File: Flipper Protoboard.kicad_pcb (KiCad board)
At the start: 2 copper layers, 71.1 x 45.7 mm, 394 parts

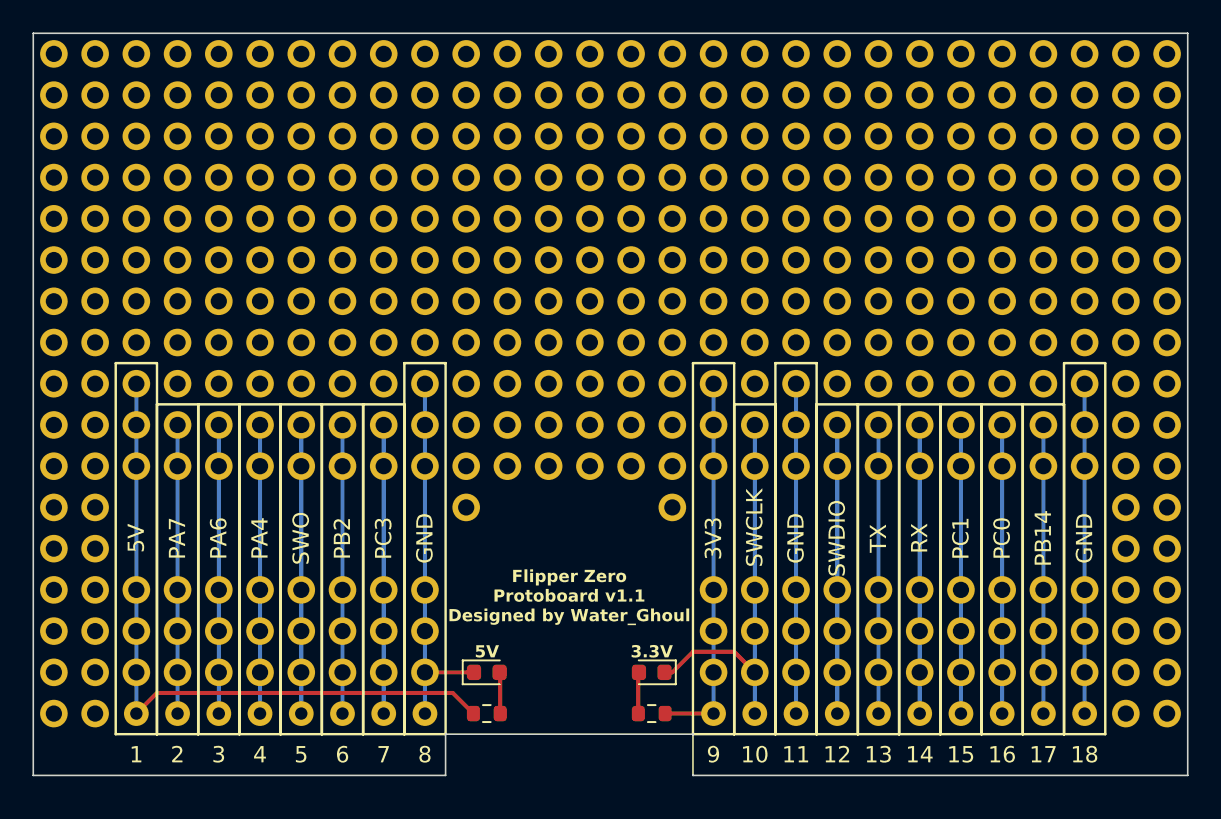
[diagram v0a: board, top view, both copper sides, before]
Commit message: Added new PCB flie
Added a few minor tweaks to update the board to v1.2
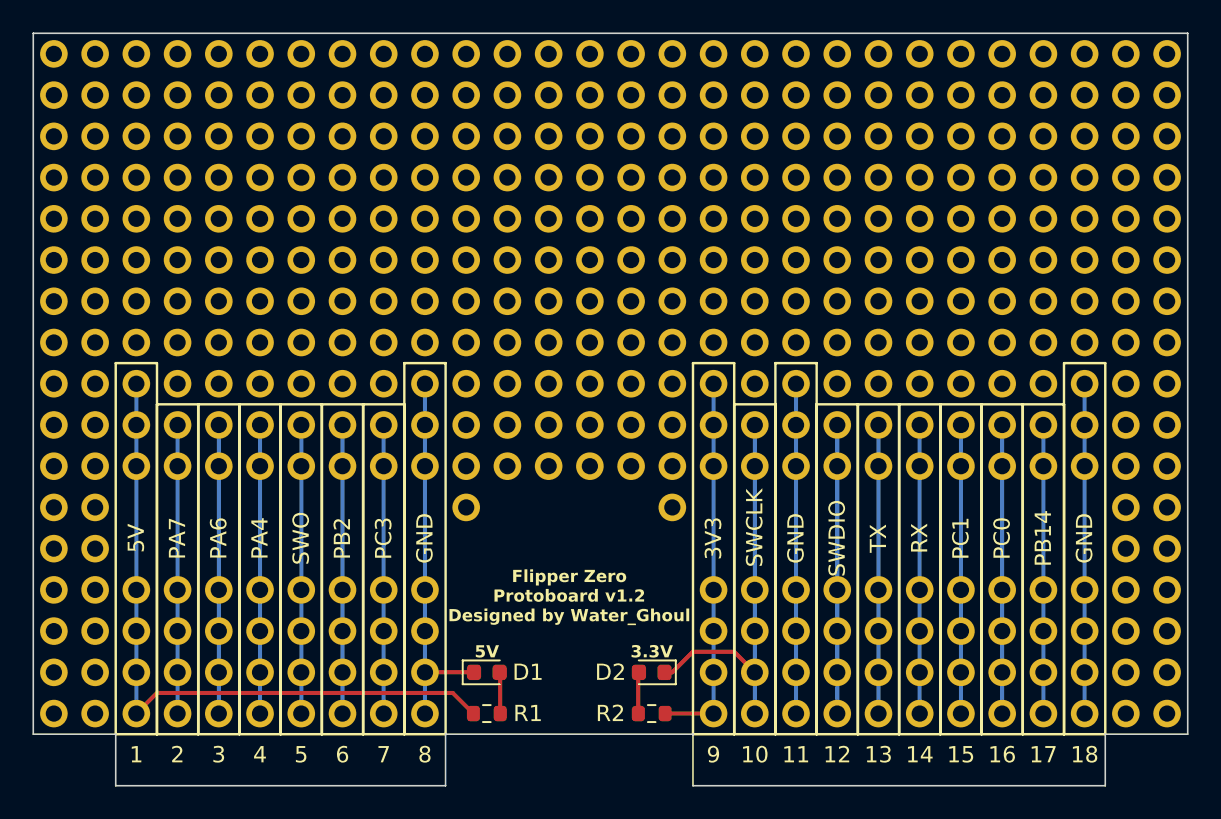
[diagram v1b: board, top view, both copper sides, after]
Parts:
- removed REF**: Flipper Zero GPIO, 1 My Parts:Flipper Zero GPIO
- added J1: PinHeader_1x08_P2.54mm_Horizontal, Connector_PinHeader_2.54mm:PinHeader_1x08_P2.54mm_Horizontal, B.Cu at (68.6, 139.7)
- added J2: PinHeader_1x10_P2.54mm_Horizontal, Connector_PinHeader_2.54mm:PinHeader_1x10_P2.54mm_Horizontal, B.Cu at (104.1, 139.7)
- renumbered REF** to D1, REF** to D2, REF** to R1, REF** to R2
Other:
- board size 71.1 x 45.7 mm -> 71.1 x 46.4 mm
- board text added: "Flipper Zero Protoboard v1.2 Designed by Water_Ghoul"
- board text removed: "Flipper Zero Protoboard v1.1 Designed by Water_Ghoul"

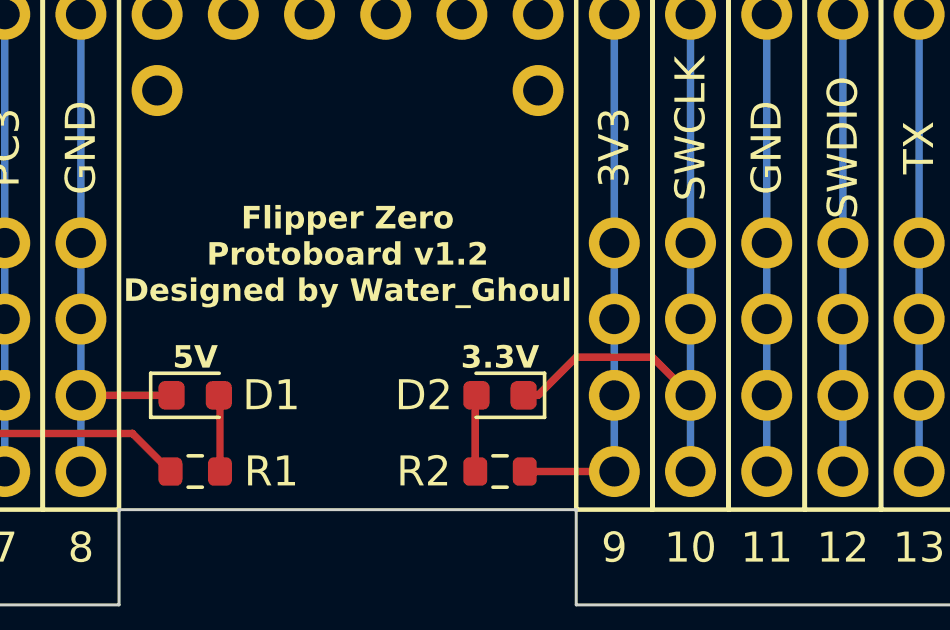
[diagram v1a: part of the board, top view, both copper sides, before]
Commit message: Fixed 3V3 LED
Fixed the 3V3 indicator LED grounded to to wrong pin.
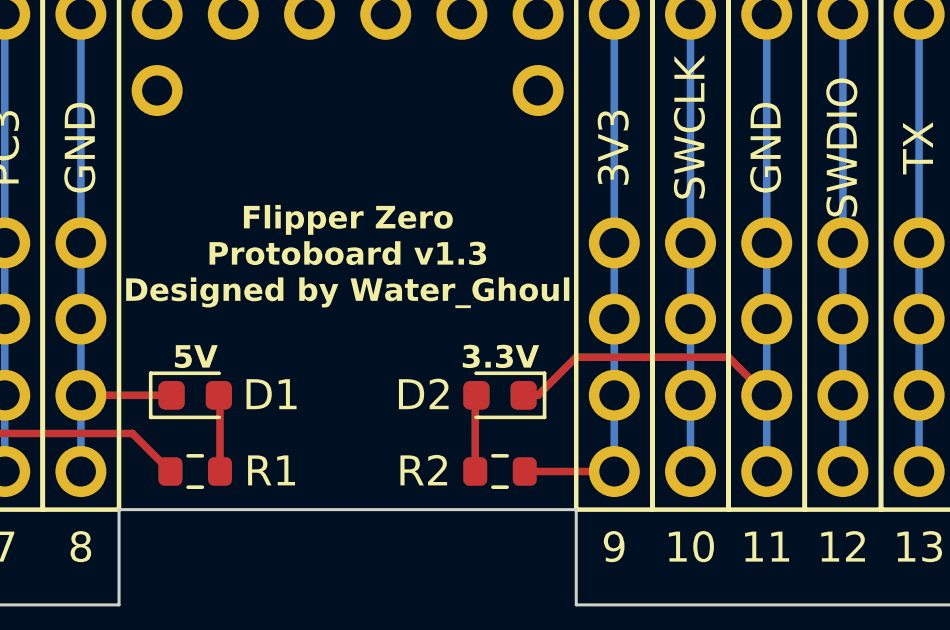
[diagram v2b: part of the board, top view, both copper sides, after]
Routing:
- net (no net): track 372.3 -> 374.8 mm
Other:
- board text added: "Flipper Zero Protoboard v1.3 Designed by Water_Ghoul"
- board text removed: "Flipper Zero Protoboard v1.2 Designed by Water_Ghoul"
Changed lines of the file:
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@@
       (plotinvisibletext false)
       (sketchpadsonfab false)
-      (subtractmaskfromsilk false)
+      (subtractmaskfromsilk true)
       (outputformat 1)
       (mirror false)
       (drillshape 0)
       (scaleselection 1)
-      (outputdirectory "Mini Gerbers/")
+      (outputdirectory "v1.2/Mini/")
     )
   )
@@
     (effects (font (size 1 1) (thickness 0.15)))
   )
-  (gr_text "Flipper Zero\nProtoboard v1.2\nDesigned by Water_Ghoul" (at 95.25 130.81) (layer "F.SilkS")
+  (gr_text "Flipper Zero\nProtoboard v1.3\nDesigned by Water_Ghoul" (at 95.25 130.81) (layer "F.SilkS")
     (effects (font (size 0.75 0.75) (thickness 0.1875) bold) (justify top))
   )
@@
     (effects (font (size 1 1) (thickness 0.15)))
   )
-  (segment (start 101.1175 137.16) (end 101.6 137.16) (width 0.25) (layer "F.Cu") (net 0))
+  (segment (start 102.87 135.89) (end 107.95 135.89) (width 0.25) (layer "F.Cu") (net 0))
   (segment (start 68.58 139.7) (end 69.85 138.43) (width 0.25) (layer "F.Cu") (net 0))
   (segment (start 90.995 139.7) (end 90.995 137.1975) (width 0.25) (layer "F.Cu") (net 0))
-  (segment (start 101.6 137.16) (end 102.87 135.89) (width 0.25) (layer "F.Cu") (net 0))
+  (segment (start 107.95 135.89) (end 109.22 137.16) (width 0.25) (layer "F.Cu") (net 0))
+  (segment (start 101.1175 137.16) (end 101.6 137.16) (width 0.25) (layer "F.Cu") (net 0))
   (segment (start 104.14 139.7) (end 101.155 139.7) (width 0.25) (layer "F.Cu") (net 0))
   (segment (start 69.85 138.43) (end 88.075 138.43) (width 0.25) (layer "F.Cu") (net 0))
   (segment (start 99.505 137.1975) (end 99.5425 137.16) (width 0.25) (layer "F.Cu") (net 0))
-  (segment (start 105.41 135.89) (end 106.68 137.16) (width 0.25) (layer "F.Cu") (net 0))
   (segment (start 88.075 138.43) (end 89.345 139.7) (width 0.25) (layer "F.Cu") (net 0))
   (segment (start 99.505 139.7) (end 99.505 137.1975) (width 0.25) (layer "F.Cu") (net 0))
-  (segment (start 102.87 135.89) (end 105.41 135.89) (width 0.25) (layer "F.Cu") (net 0))
   (segment (start 89.3825 137.16) (end 86.36 137.16) (width 0.25) (layer "F.Cu") (net 0))
+  (segment (start 101.6 137.16) (end 102.87 135.89) (width 0.25) (layer "F.Cu") (net 0))
   (segment (start 90.995 137.1975) (end 90.9575 137.16) (width 0.25) (layer "F.Cu") (net 0))
   (segment (start 106.68 139.7) (end 106.68 121.92) (width 0.25) (layer "B.Cu") (net 0))
